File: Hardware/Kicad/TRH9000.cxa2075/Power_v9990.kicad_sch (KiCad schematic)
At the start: 17 parts, among them U1 74HC138, U2 74HC32, U3 V9990, U4 KM428C256, U5 KM428C256

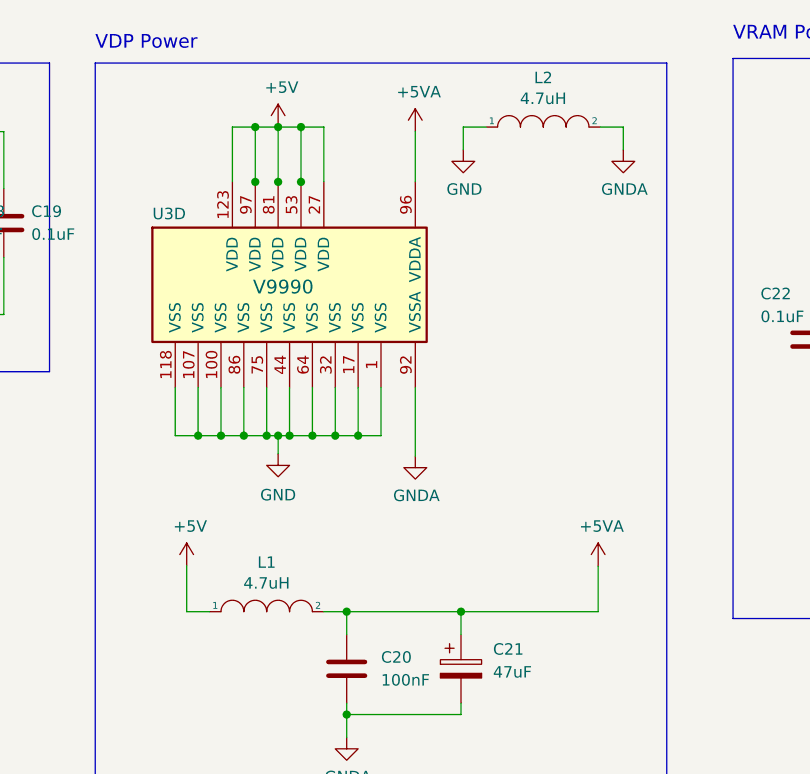
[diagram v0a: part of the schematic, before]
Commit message: small fix on the YTRAP to use internal for NTSC.
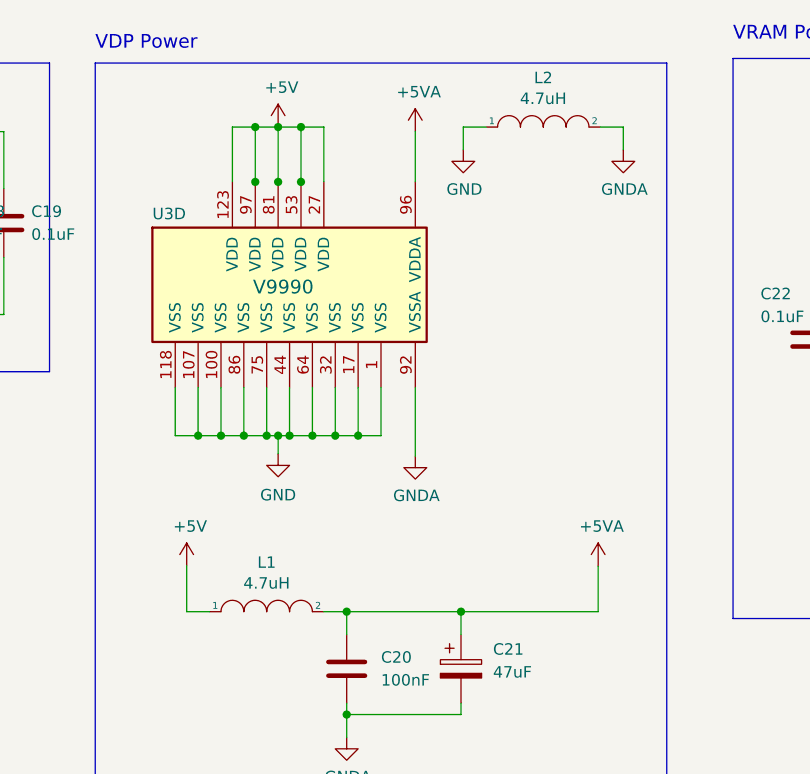
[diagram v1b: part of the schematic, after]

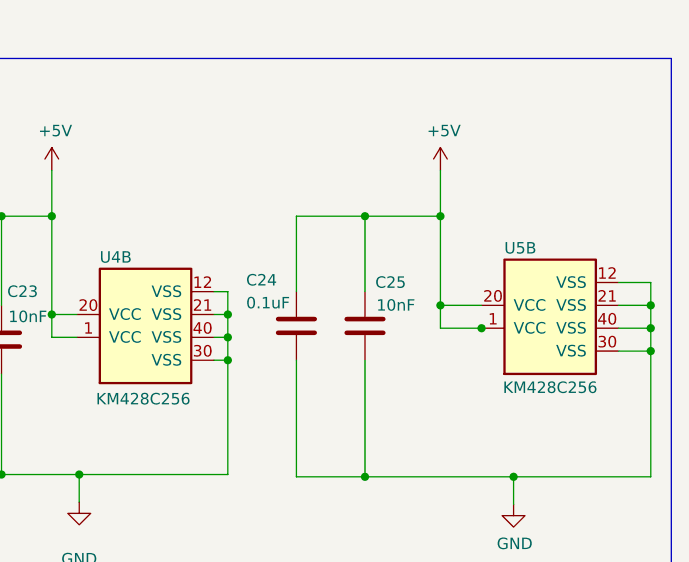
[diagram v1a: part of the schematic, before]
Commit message: Fix on VRAM wiring
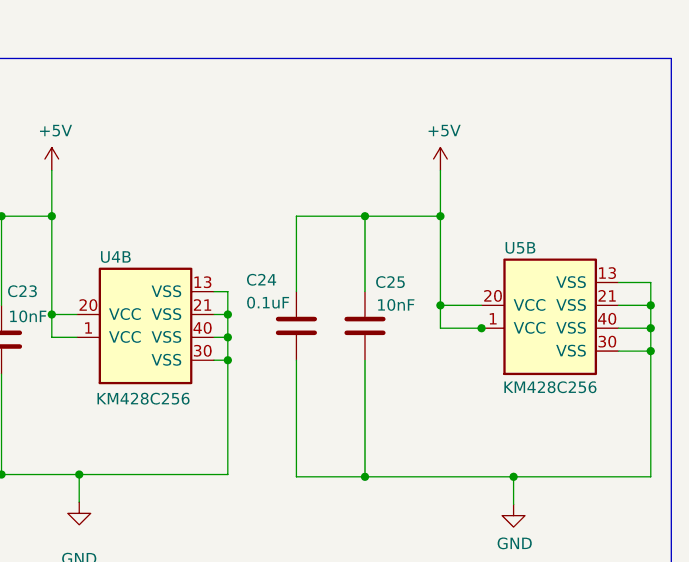
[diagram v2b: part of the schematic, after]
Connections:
- net GND: now also U4.13 (VSS), U5.13 (VSS); no longer U4.12 (VSS), U5.12 (VSS)
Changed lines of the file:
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@@
   (title_block
     (title "TRH9000")
-    (date "2022-12-26")
-    (rev "1.2")
+    (date "2023-10-22")
+    (rev "1.3")
     (company "The Retro Hacker")
     (comment 2 "Shared under CERN-OHL-S license")
@@
     (pin "10")
     (pin "11")
-    (pin "13")
+    (pin "12")
     (pin "14")
     (pin "15")
@@
     (pin "9")
     (pin "1")
-    (pin "12")
+    (pin "13")
     (pin "20")
     (pin "21")
@@
     (pin "10")
     (pin "11")
-    (pin "13")
+    (pin "12")
     (pin "14")
     (pin "15")
@@
     (pin "9")
     (pin "1")
-    (pin "12")
+    (pin "13")
     (pin "20")
     (pin "21")

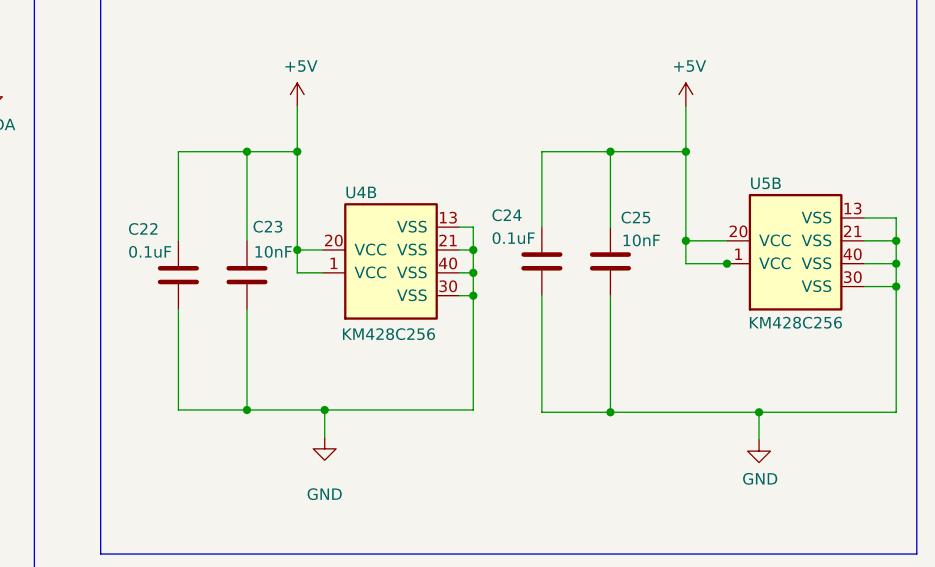
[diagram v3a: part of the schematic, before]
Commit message: Fix on pins 12 and 13 of the VRAM
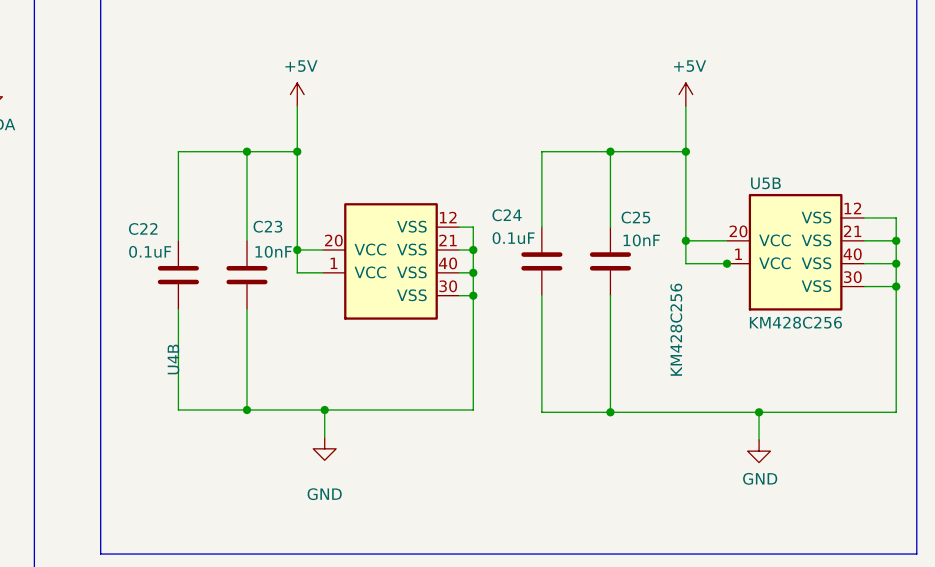
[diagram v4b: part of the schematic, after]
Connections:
- net GND: now also U4.12 (VSS), U5.12 (VSS); no longer U4.13 (VSS), U5.13 (VSS)
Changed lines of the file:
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@@
 (kicad_sch (version 20230121) (generator eeschema)
-  (paper "A4")
+  (paper "A3")
   (title_block
     (title "TRH9000")
-    (date "2023-11-05")
-    (rev "1.4")
+    (date "2024-03-19")
+    (rev "1.6")
     (company "The Retro Hacker")
     (comment 2 "Shared under CERN-OHL-S license")
@@
   (symbol (lib_name "KM428C256_1") (lib_id "TRH9000:KM428C256") (at 218.694 55.88 90) (unit 2)
     (in_bom yes) (on_board yes) (dnp no)
-    (property "Reference" "U4" (at 217.17 46.99 90)
-      (effects (font (size 1.27 1.27)) (justify left))
-    )
-    (property "Value" "KM428C256" (at 218.44 62.738 90)
+    (property "Reference" "U4" (at 194.564 67.31 0)
+      (effects (font (size 1.27 1.27)) (justify left))
+    )
+    (property "Value" "KM428C256" (at 250.444 62.23 0)
       (effects (font (size 1.27 1.27)))
     )
@@
     (pin "10")
     (pin "11")
-    (pin "12")
+    (pin "13")
     (pin "14")
     (pin "15")
@@
     (pin "9")
     (pin "1")
-    (pin "13")
+    (pin "12")
     (pin "20")
     (pin "21")
@@
           (reference "U4") (unit 2)
         )
+        (path "/1a0ec755-0979-4213-9180-0cd879831c1c/d5c7e94e-ee8c-4fa2-b6f9-333fadc34caa"
+          (reference "U4") (unit 2)
+        )
       )
     )
@@
     (pin "10")
     (pin "11")
-    (pin "12")
+    (pin "13")
     (pin "14")
     (pin "15")
@@
     (pin "9")
     (pin "1")
-    (pin "13")
+    (pin "12")
     (pin "20")
     (pin "21")

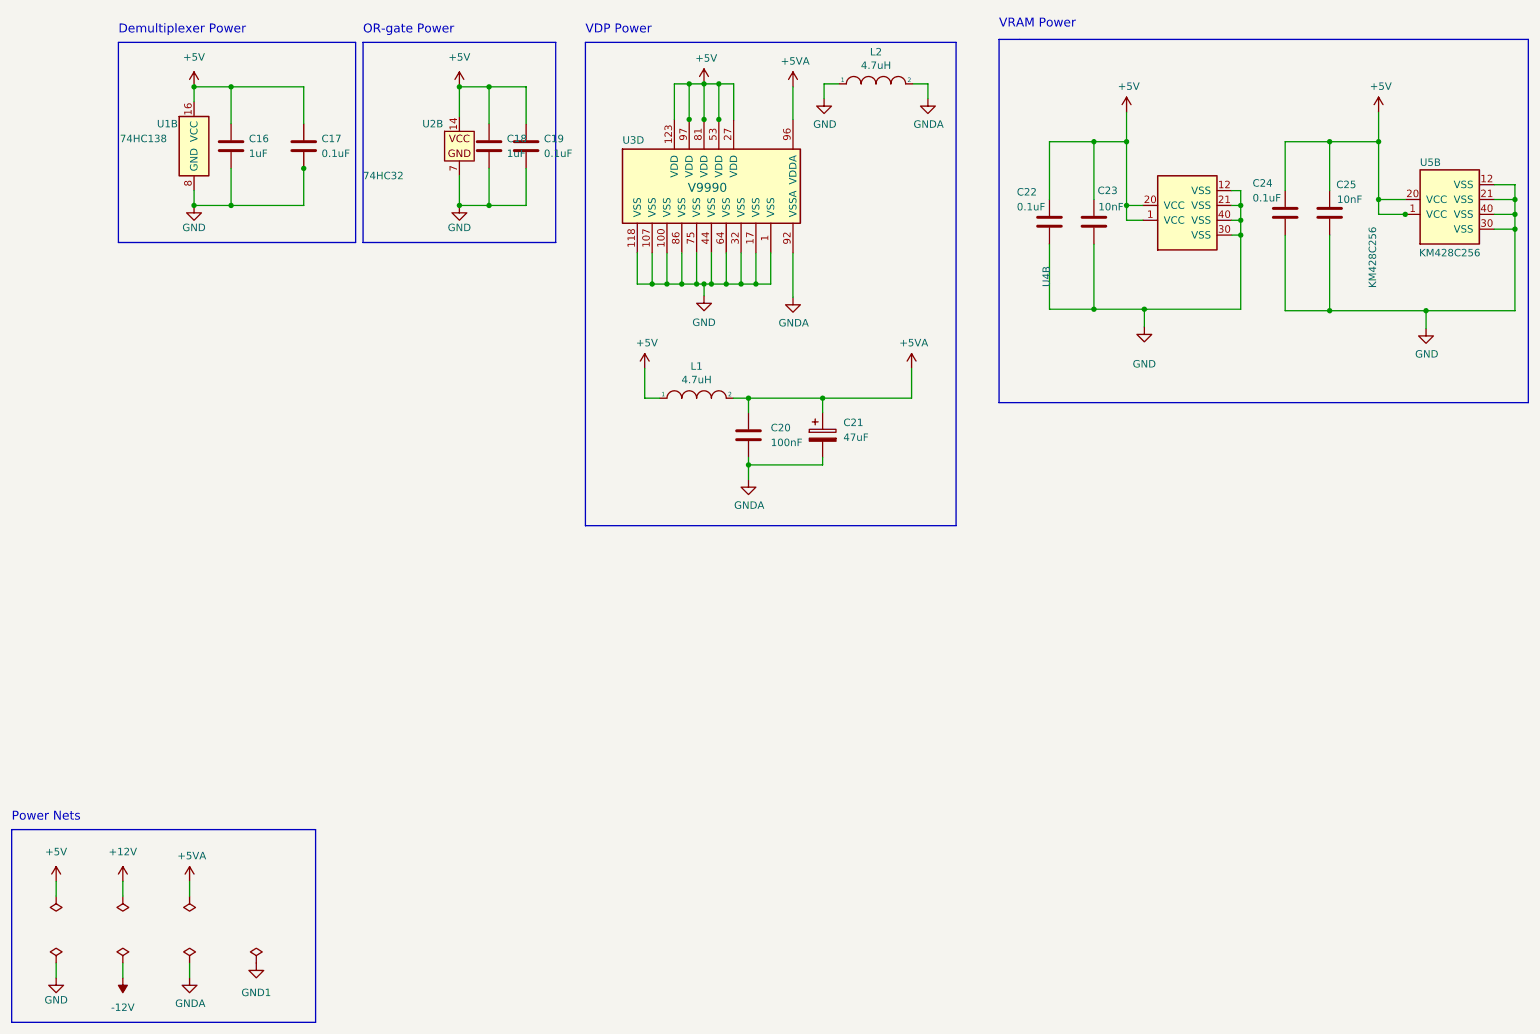
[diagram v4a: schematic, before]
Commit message: kicad 8 migration. minor positioning for the connectors
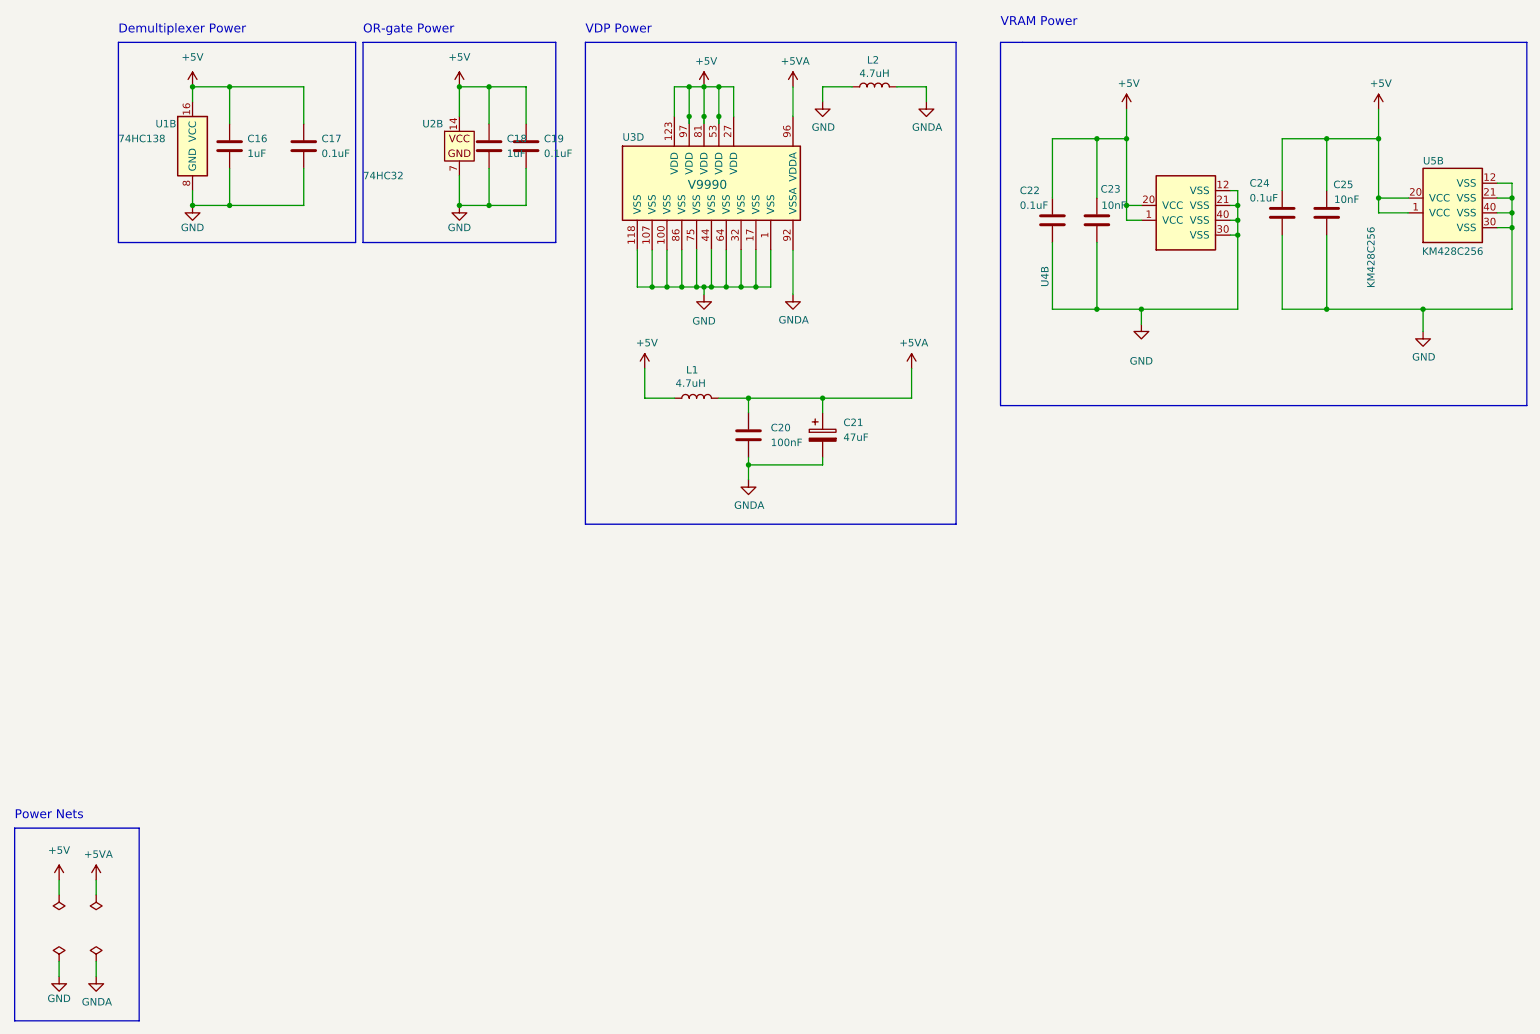
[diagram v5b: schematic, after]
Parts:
- L1, L2: symbol pspice:INDUCTOR -> Device:L
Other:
- moved on the sheet: C22, C23, C24, C25, U3D, U5B
